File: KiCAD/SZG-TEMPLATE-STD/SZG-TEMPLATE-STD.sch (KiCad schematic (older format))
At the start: 28 parts, among them J1 SYZYGY_STD, J2 Conn_01x06, U1 ATtiny44A-MU

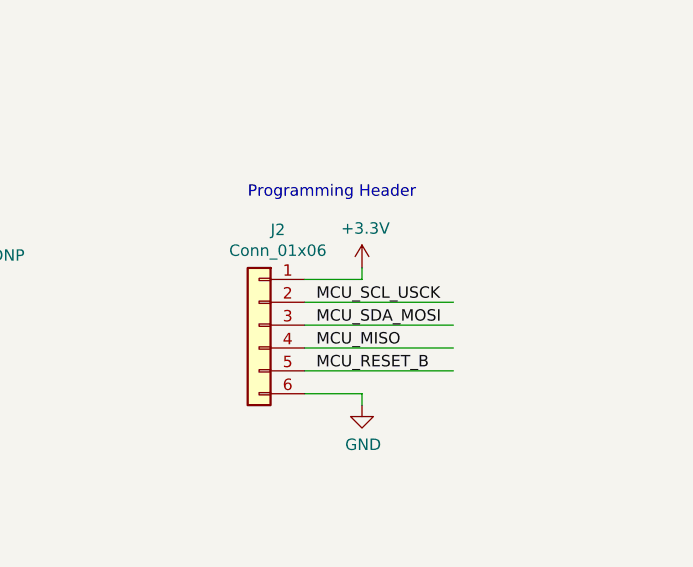
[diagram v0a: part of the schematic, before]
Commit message: Updated the template projects MCU programming header to use the standard Tag-Connect cable pin order.
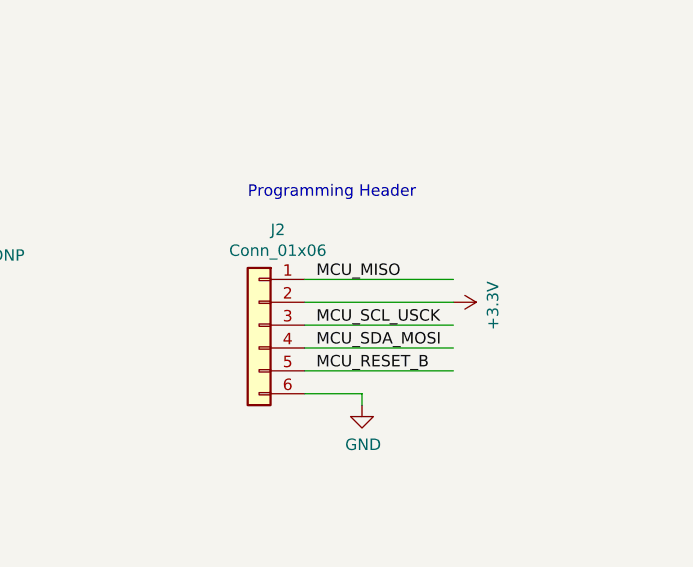
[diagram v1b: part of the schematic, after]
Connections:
- wire segments 72 -> 71
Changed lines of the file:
@@
 Wire Wire Line
 	6500 3500 7150 3500
-Text Label 9550 3300 0    50   ~ 0
+Text Label 9550 3400 0    50   ~ 0
 MCU_SCL_USCK
+Text Label 9550 3200 0    50   ~ 0
+MCU_MISO
 Text Label 9550 3500 0    50   ~ 0
-MCU_MISO
-Text Label 9550 3400 0    50   ~ 0
 MCU_SDA_MOSI
 Wire Wire Line
@@
 L power:+3.3V #PWR0110
 U 1 1 60652346
-P 9750 3150
-F 0 "#PWR0110" H 9750 3000 50  0001 C CNN
-F 1 "+3.3V" H 9765 3323 50  0000 C CNN
-F 2 "" H 9750 3150 50  0001 C CNN
-F 3 "" H 9750 3150 50  0001 C CNN
-	1    9750 3150
-	1    0    0    -1
+P 10150 3300
+F 0 "#PWR0110" H 10150 3150 50  0001 C CNN
+F 1 "+3.3V" H 10165 3473 50  0000 C CNN
+F 2 "" H 10150 3300 50  0001 C CNN
+F 3 "" H 10150 3300 50  0001 C CNN
+	1    10150 3300
+	0    1    1    0
 $EndComp
 $Comp
@@
 	-1   0    0    -1
 $EndComp
-Wire Wire Line
-	9500 3200 9750 3200
-Wire Wire Line
-	9750 3200 9750 3150
 Wire Wire Line
 	9500 3700 9750 3700
@@
 EndData
 $EndBitmap
+Wire Wire Line
+	9500 3200 10150 3200
 $EndSCHEMATC
